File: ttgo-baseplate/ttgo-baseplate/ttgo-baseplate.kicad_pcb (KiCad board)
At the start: 2 copper layers, 55.1 x 76.6 mm, 4 parts, among them J1 Conn_02x16_Odd_Even, J2 Conn_02x16_Odd_Even, J3 Conn_02x10_Odd_Even, J4 Conn_01x05

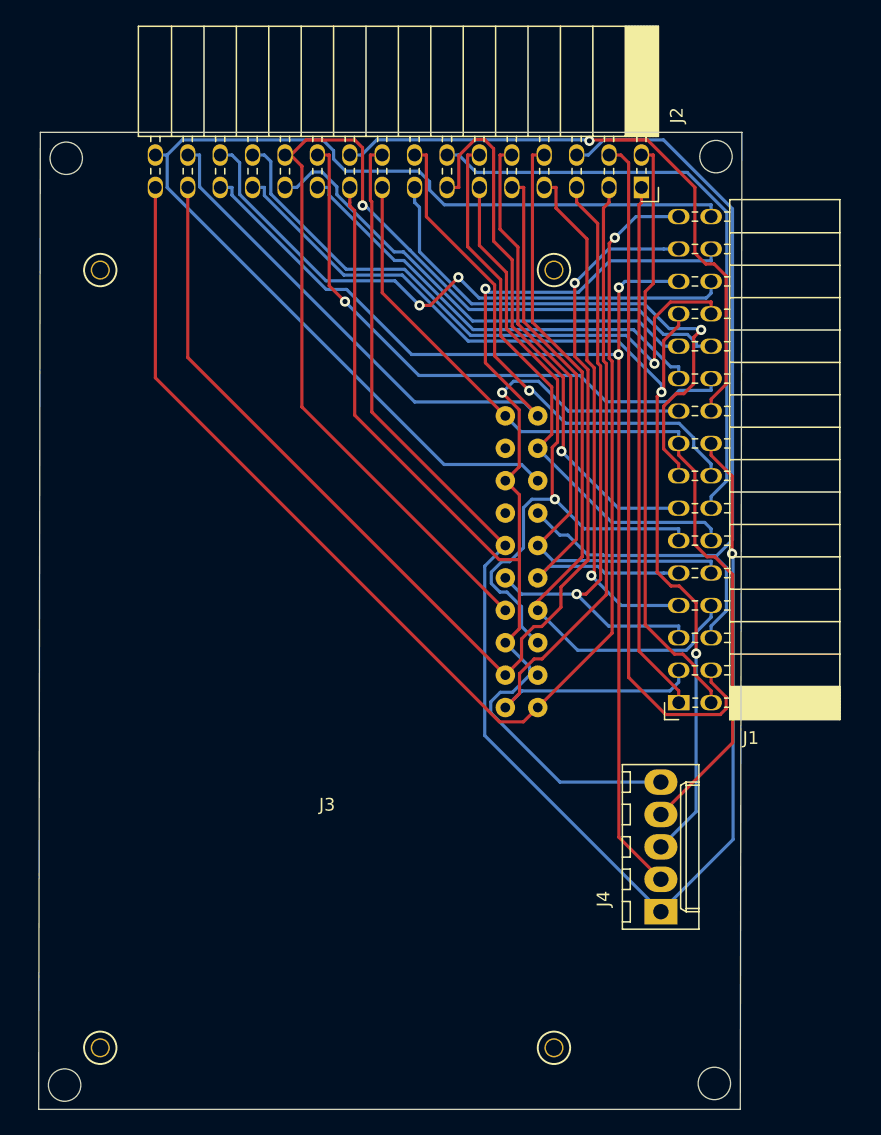
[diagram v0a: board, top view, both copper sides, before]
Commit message: ttgo baseplate rerouted
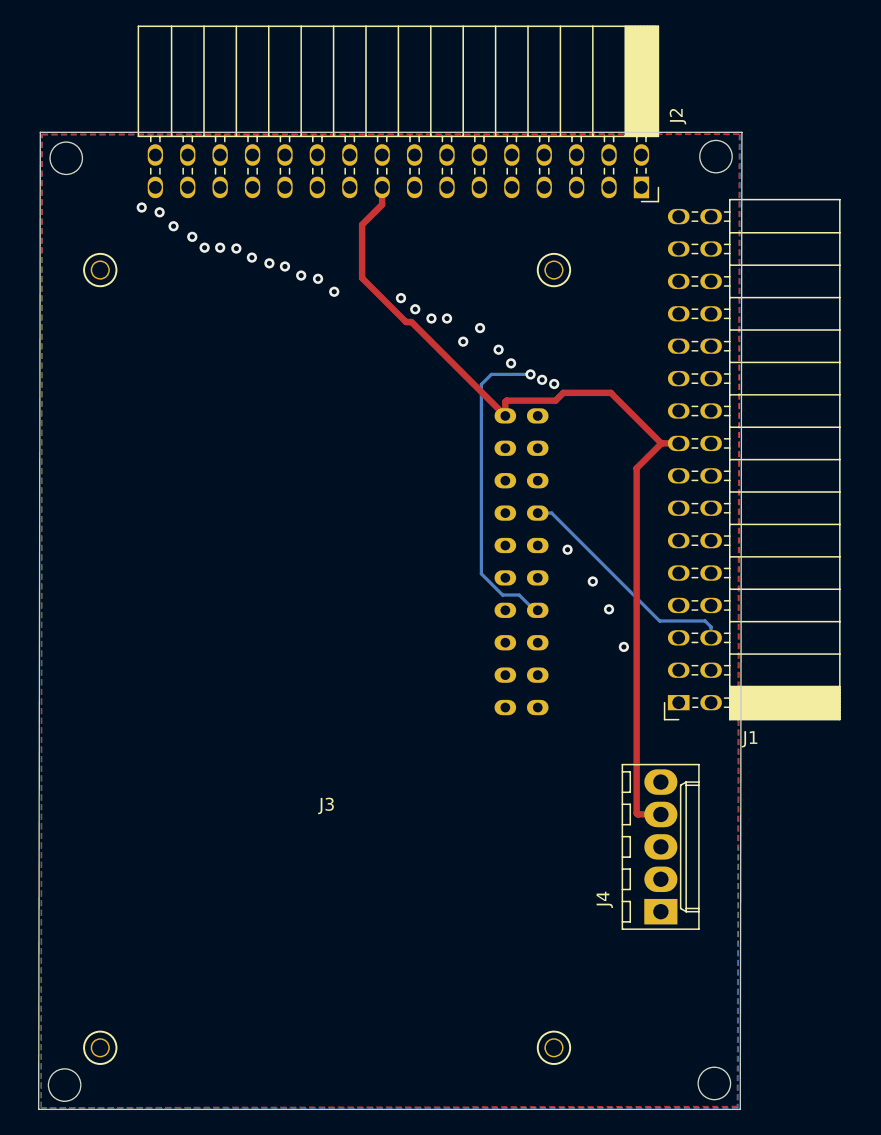
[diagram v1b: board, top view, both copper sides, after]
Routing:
- net /3.3V: track 110.8 -> 0.00 mm, vias 1 -> 0
- net /GND: track 96.6 -> 0.25 mm, vias 1 -> 0
- net /SVP: track 68.8 -> 91.6 mm
- net /IO35: track 49.9 -> 67.0 mm, vias 0 -> 1
- net /SVN: track 44.2 -> 60.6 mm, vias 0 -> 1
- net /IO33: track 56.9 -> 71.0 mm, vias 0 -> 1
- net /IO32: track 46.1 -> 58.5 mm, vias 0 -> 1
- net /IO25: track 55.4 -> 64.7 mm
- net /TMS: track 54.7 -> 46.9 mm, vias 0 -> 1
- net /IO00: track 60.0 -> 53.4 mm, vias 0 -> 1
- net /IO18: track 49.2 -> 55.1 mm
- net /SCL: track 89.7 -> 95.5 mm, vias 2 -> 1
- net /TCK: track 40.7 -> 46.0 mm
- net /IO27: track 44.0 -> 38.9 mm
- net /TXD: track 101.7 -> 97.7 mm
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- added copper zone on F.Cu, net /3.3V
- added copper zone on B.Cu, net /GND
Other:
- copper layers 2 -> 4
- net class Power added: clearance 0.35, trace_width 0.25, via_dia 0.8, via_drill 0.4

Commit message: gnd en 3v3 panes in center now
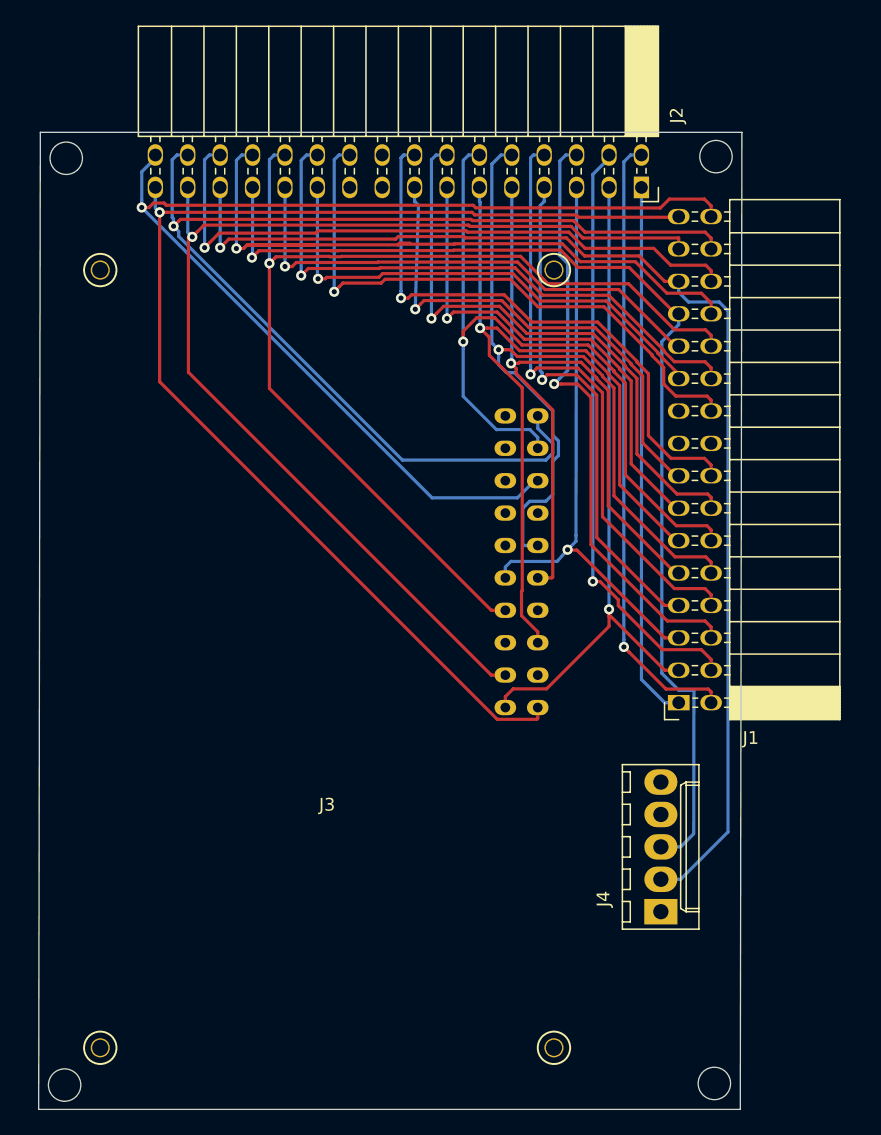
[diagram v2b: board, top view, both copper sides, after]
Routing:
- added copper zone on In1.Cu, net /3.3V
- added copper zone on In2.Cu, net /GND
- removed copper zone on F.Cu, net /3.3V
- removed copper zone on B.Cu, net /GND

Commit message: - Adjusted T4 size and drilling holes on footprint - Changed footprint of the TTGO T4 expansion connector to match pn numbering of schematic. - Signals on the TTGO T4 were mirrorred top bottom, corrected order. - TTGO-T4 to Wemos mapping was not followed making most Dx signals on the inner Wemos connector unusable. - Added jumpers to replace I2C by other signals. Cut them if you want to use the I2C connector on the board. - Added ground planes at both sides. Board is now 2 layers. - Used proper drill holes. The mounting holes did not appear in a drilling file. Not a clue if they can be done as an edge cut. But this will certainly work.\ - Lots of small changes hre and there.
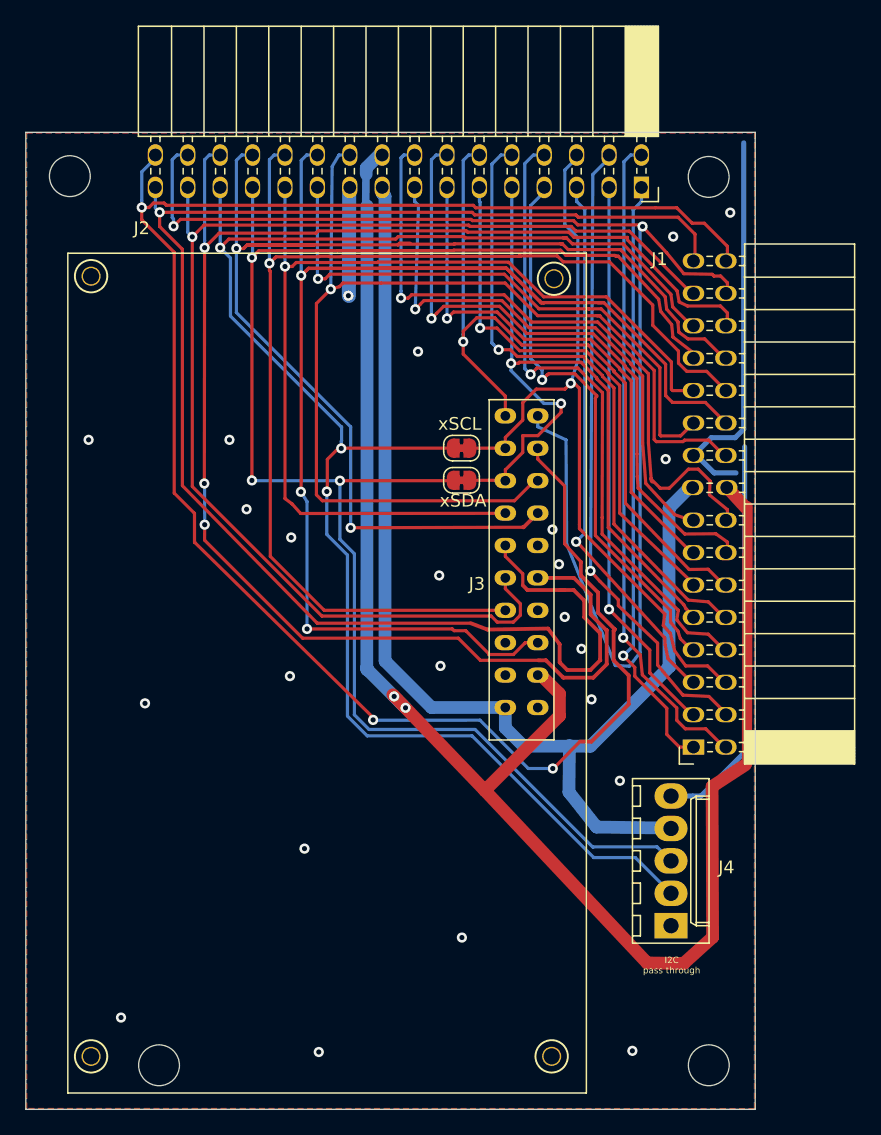
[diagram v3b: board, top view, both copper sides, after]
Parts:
- added MH1: MountingHole, MountingHole:MountingHole_3.2mm_M3, F.Cu at (166.1, 75.6)
- added MH2: MountingHole, MountingHole:MountingHole_3.2mm_M3, F.Cu at (166.1, 145.3)
- added MH3: MountingHole, MountingHole:MountingHole_3.2mm_M3, F.Cu at (116.0, 75.6)
- added MH4: MountingHole, MountingHole:MountingHole_3.2mm_M3, F.Cu at (123.0, 145.3)
- added xSCL: SCL, Jumper:SolderJumper-2_P1.3mm_Bridged_RoundedPad1.0x1.5mm, F.Cu at (146.7, 96.9)
- added xSDA: SDA, Jumper:SolderJumper-2_P1.3mm_Bridged_RoundedPad1.0x1.5mm, F.Cu at (146.7, 99.4)
- moved J1 3.67 mm to (164.9, 120.3)
- moved J4 1.35 mm to (163.1, 134.3)
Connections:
- J3 pad 1: /5V -> /SVN
- J3 pad 10: /IO00 -> /5V
- J3 pad 11: /TXD -> Net-(J3-Pad11)
- J3 pad 12: /GND -> /3.3V
- J3 pad 13: /IO25 -> /IO23
- J3 pad 14: /IO33 -> /GND
- J3 pad 15: /IO32 -> /IO26
- J3 pad 16: /IO35 -> /GND
- J3 pad 17: /IO34 -> /IO18
- J3 pad 18: /RST -> /IO05
- J3 pad 19: /SVN -> /RST
- J3 pad 2: (no net) -> /IO34
- J3 pad 3: /GND -> /IO32
- J3 pad 4: (no net) -> /IO17
- J3 pad 5: /3.3V -> /TXD
- J3 pad 6: /IO04 -> /RXD
- J3 pad 8: /GND -> Net-(J3-Pad8)
- J3 pad 9: /RXD -> /GND
- J4 pad 1: /3.3V -> Net-(J4-Pad1)
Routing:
- net /3.3V: track 0.00 -> 130.6 mm, vias 0 -> 2
- net /IO23: track 47.0 -> 123.7 mm, vias 1 -> 3
- net /IO26: track 50.7 -> 126.1 mm, vias 1 -> 3
- net /GND: track 0.25 -> 71.2 mm, vias 0 -> 24
- net /RST: track 91.9 -> 148.1 mm, vias 1 -> 3
- net /IO18: track 55.1 -> 99.2 mm, vias 1 -> 2
- net /IO17: track 39.9 -> 80.0 mm
- net /SDA: track 87.3 -> 127.0 mm, vias 1 -> 3
- net /IO05: track 47.2 -> 86.6 mm
- net /SCL: track 95.5 -> 128.2 mm, vias 1 -> 3
- net /TXD: track 97.7 -> 123.5 mm
- net /IO25: track 64.7 -> 42.1 mm
- net /5V: track 72.3 -> 94.0 mm
- net /IO33: track 71.0 -> 50.4 mm
- net /SVP: track 91.6 -> 111.0 mm, vias 1 -> 2
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- added copper zone on B.Cu, net /GND
- added copper zone on F.Cu, net /GND
- removed copper zone on In1.Cu, net /3.3V
- removed copper zone on In2.Cu, net /GND
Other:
- board size 55.1 x 76.6 mm -> 57.2 x 76.6 mm
- copper layers 4 -> 2
- board text added: "I2C pass through"
- board text added: "SenseMakers Amsterdam - in2tech"
- board text added: "TTGO-T4-Base Plate"
- board text added: "k.wessing@in2tech.nl"
- board text added: "rev 1.1 10/02/2020"
